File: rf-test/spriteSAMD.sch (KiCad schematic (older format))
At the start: 7 parts, among them J1 Conn_01x08_Female, J2 Conn_Coaxial, J3 Conn_01x08_Female, U8 RFM95W-915S2

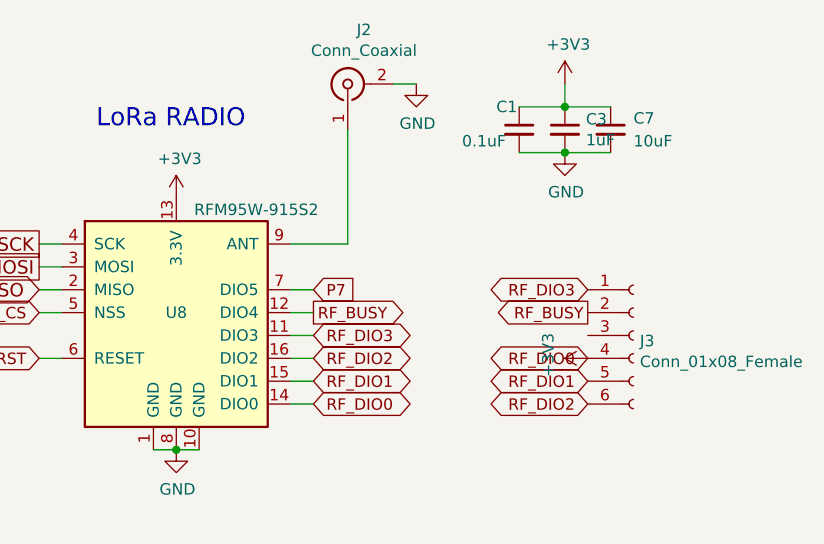
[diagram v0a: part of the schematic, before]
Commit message: Fixed Mistake in RF Test Board
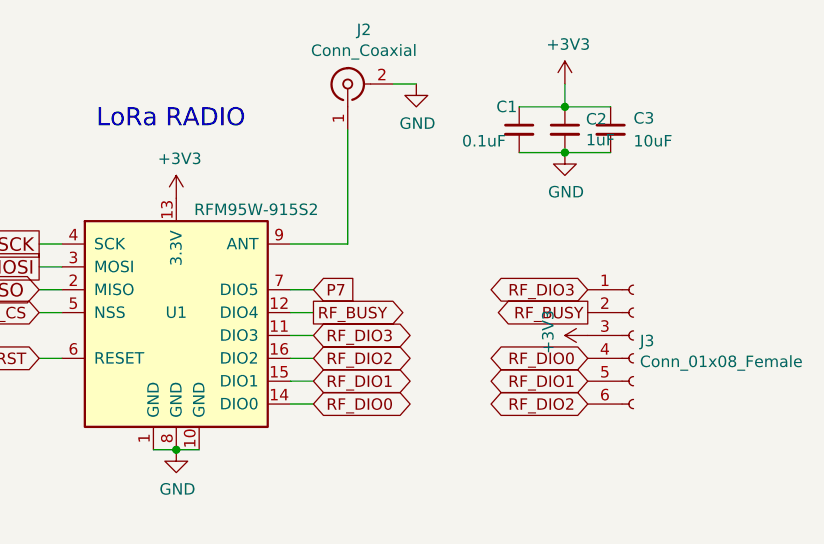
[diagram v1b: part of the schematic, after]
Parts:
- renumbered C3 to C2, C7 to C3, U8 to U1
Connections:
- net +3V3: now also J3.3 (Pin_3); no longer J3.4 (Pin_4), U1.14 (DIO0)
- new net RF_DIO0: J3.4 (Pin_4), U1.14 (DIO0)
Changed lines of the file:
@@
 $EndComp
 $Comp
-L Device:C_Small C7
+L Device:C_Small C3
 U 1 1 5DA4FC48
 P 6200 3000
-F 0 "C7" H 6300 3050 50  0000 L CNN
+F 0 "C3" H 6300 3050 50  0000 L CNN
 F 1 "10uF" H 6300 2950 50  0000 L CNN
 F 2 "Capacitor_SMD:C_0402_1005Metric" H 6200 3000 50  0001 C CNN
@@
 Connection ~ 6000 2900
 $Comp
-L power:+3V3 #PWR0110
+L power:+3V3 #PWR05
 U 1 1 5DA85869
 P 6000 2800
-F 0 "#PWR0110" H 6000 2650 50  0001 C CNN
+F 0 "#PWR05" H 6000 2650 50  0001 C CNN
 F 1 "+3V3" H 6015 2973 50  0000 C CNN
 F 2 "" H 6000 2800 50  0001 C CNN
@@
 	6000 2800 6000 2900
 $Comp
-L Device:C_Small C3
+L Device:C_Small C2
 U 1 1 5D1C3FDB
 P 6000 3000
-F 0 "C3" H 6092 3046 50  0000 L CNN
+F 0 "C2" H 6092 3046 50  0000 L CNN
 F 1 "1uF" H 6092 2955 50  0000 L CNN
 F 2 "Capacitor_SMD:C_0402_1005Metric" H 6000 3000 50  0001 C CNN
@@
 	6000 3100 6200 3100
 $Comp
-L power:GND #PWR0118
+L power:GND #PWR06
 U 1 1 5D1CCAB1
 P 6000 3100
-F 0 "#PWR0118" H 6000 2850 50  0001 C CNN
+F 0 "#PWR06" H 6000 2850 50  0001 C CNN
 F 1 "GND" H 6005 2927 50  0000 C CNN
 F 2 "" H 6000 3100 50  0001 C CNN
@@
 Sprite LoRa Generic
 $Comp
-L RF_Module:RFM95W-915S2 U8
+L RF_Module:RFM95W-915S2 U1
 U 1 1 5D188C92
 P 4300 3800
-F 0 "U8" H 4300 3800 50  0000 C CNN
+F 0 "U1" H 4300 3800 50  0000 C CNN
 F 1 "RFM95W-915S2" H 4650 4250 50  0000 C CNN
 F 2 "RF_Module:HOPERF_RFM9XW_SMD" H 1000 5450 50  0001 C CNN
@@
 RF_DIO2
 $Comp
-L power:GND #PWR0140
+L power:GND #PWR03
 U 1 1 5D1CBF31
 P 4300 4400
-F 0 "#PWR0140" H 4300 4150 50  0001 C CNN
+F 0 "#PWR03" H 4300 4150 50  0001 C CNN
 F 1 "GND" H 4305 4227 50  0000 C CNN
 F 2 "" H 4300 4400 50  0001 C CNN
@@
 	4300 4400 4400 4400
 $Comp
-L power:+3V3 #PWR0141
+L power:+3V3 #PWR02
 U 1 1 5D1D57F0
 P 4300 3300
-F 0 "#PWR0141" H 4300 3150 50  0001 C CNN
+F 0 "#PWR02" H 4300 3150 50  0001 C CNN
 F 1 "+3V3" H 4315 3473 50  0000 C CNN
 F 2 "" H 4300 3300 50  0001 C CNN
@@
 	5350 2800 5250 2800
 $Comp
-L power:GND #PWR0106
+L power:GND #PWR04
 U 1 1 5D1C2EFC
 P 5350 2800
-F 0 "#PWR0106" H 5350 2550 50  0001 C CNN
+F 0 "#PWR04" H 5350 2550 50  0001 C CNN
 F 1 "GND" H 5355 2627 50  0000 C CNN
 F 2 "" H 5350 2800 50  0001 C CNN
@@
 P7
 $Comp
-L power:GND #PWR0101
+L power:GND #PWR01
 U 1 1 5DB9A17D
 P 2900 4150
-F 0 "#PWR0101" H 2900 3900 50  0001 C CNN
+F 0 "#PWR01" H 2900 3900 50  0001 C CNN
 F 1 "GND" H 2905 3977 50  0000 C CNN
 F 2 "" H 2900 4150 50  0001 C CNN
@@
 Text GLabel 6100 3800 0    50   Output ~ 0
 RF_BUSY
-$Comp
-L power:+3V3 #PWR0103
-U 1 1 5DBA07F8
-P 6100 4000
-F 0 "#PWR0103" H 6100 3850 50  0001 C CNN
-F 1 "+3V3" H 6115 4173 50  0000 C CNN
-F 2 "" H 6100 4000 50  0001 C CNN
-F 3 "" H 6100 4000 50  0001 C CNN
-	1    6100 4000
-	0    -1   -1   0
-$EndComp
-Text GLabel 6100 4000 0    50   BiDi ~ 0
-RF_DIO0
 Text GLabel 6100 4100 0    50   BiDi ~ 0
 RF_DIO1
 Text GLabel 6100 4200 0    50   BiDi ~ 0
 RF_DIO2
+$Comp
+L power:+3V3 #PWR07
+U 1 1 5DBA07F8
+P 6100 3900
+F 0 "#PWR07" H 6100 3750 50  0001 C CNN
+F 1 "+3V3" H 6115 4073 50  0000 C CNN
+F 2 "" H 6100 3900 50  0001 C CNN
+F 3 "" H 6100 3900 50  0001 C CNN
+	1    6100 3900
+	0    -1   -1   0
+$EndComp
+Text GLabel 6100 4000 0    50   BiDi ~ 0
+RF_DIO0
 $EndSCHEMATC
